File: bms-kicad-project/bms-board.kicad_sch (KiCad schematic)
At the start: 0 parts

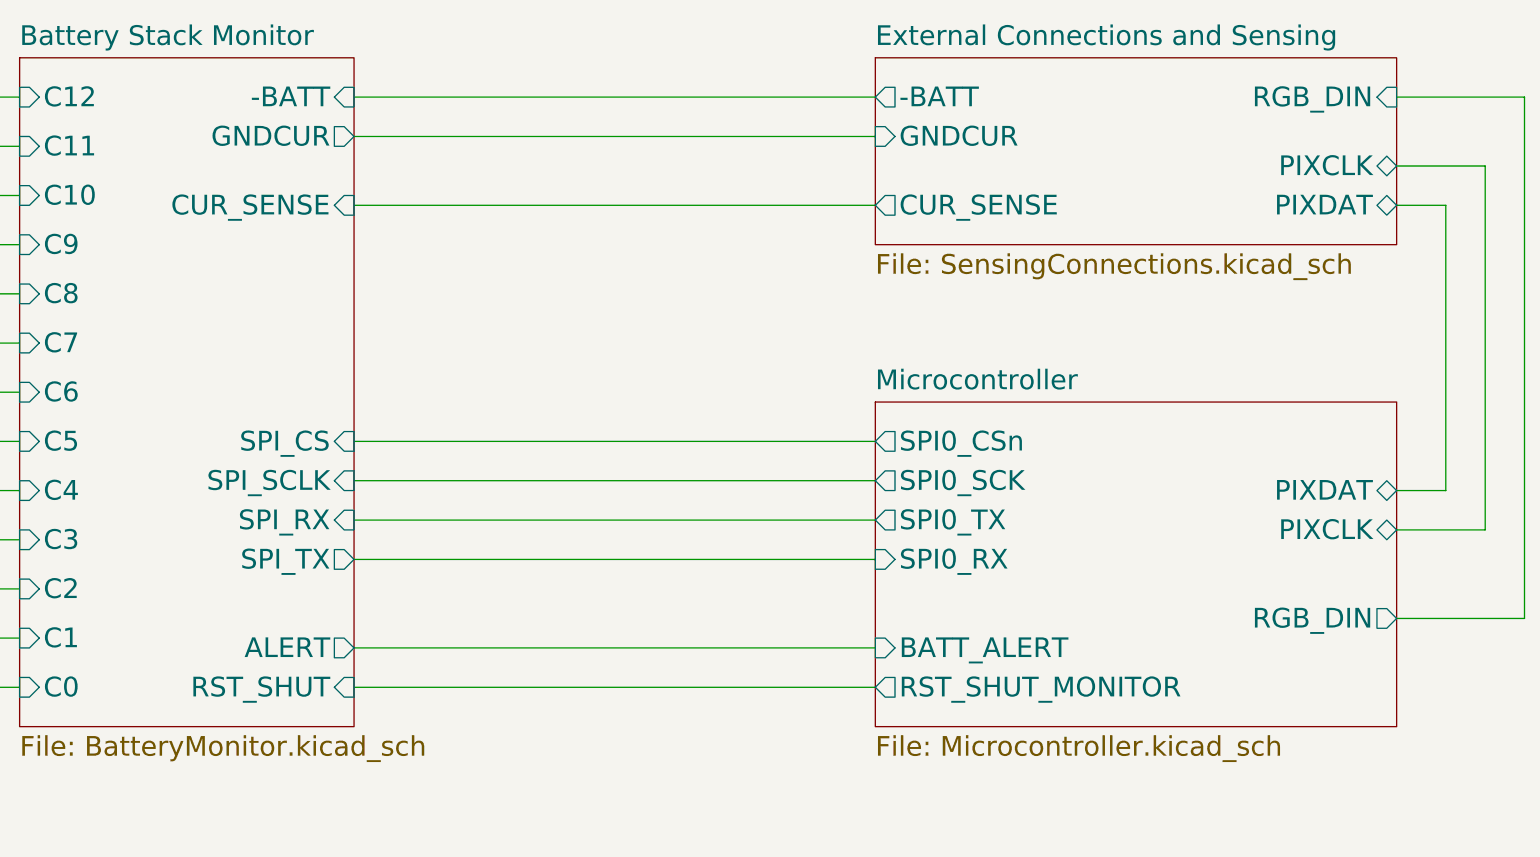
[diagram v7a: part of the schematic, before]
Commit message: feat: added current sense DAC
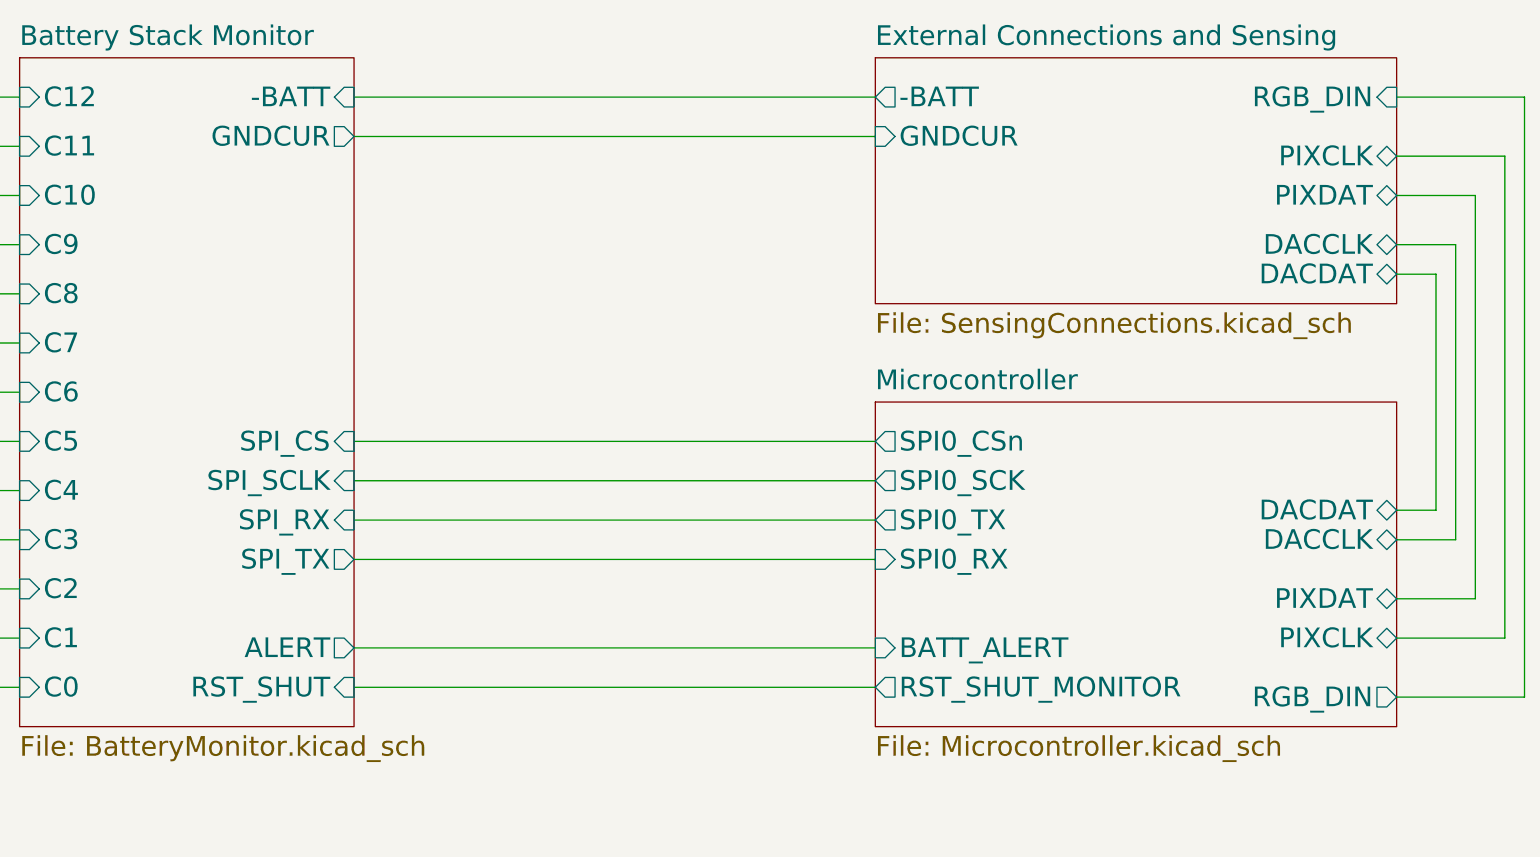
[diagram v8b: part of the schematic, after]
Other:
- sheet Battery Stack Monitor ports: added none; removed CUR_SENSE
- sheet External Connections and Sensing ports: added DACCLK, DACDAT; removed CUR_SENSE
- sheet Microcontroller ports: added DACCLK, DACDAT; removed none
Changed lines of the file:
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@@
+    (stroke (width 0) (type default))
+  )
+  (wire (pts (xy 367.03 99.06) (xy 367.03 137.16))
     (stroke (width 0) (type default))
   )
@@
     (stroke (width 0) (type default))
   )
-  (wire (pts (xy 375.92 80.01) (xy 375.92 147.32))
-    (stroke (width 0) (type default))
-  )
-  (wire (pts (xy 375.92 147.32) (xy 359.41 147.32))
-    (stroke (width 0) (type default))
-  )
-  (wire (pts (xy 370.84 135.89) (xy 370.84 88.9))
+  (wire (pts (xy 359.41 149.86) (xy 373.38 149.86))
+    (stroke (width 0) (type default))
+  )
+  (wire (pts (xy 375.92 80.01) (xy 375.92 157.48))
+    (stroke (width 0) (type default))
+  )
+  (wire (pts (xy 375.92 157.48) (xy 359.41 157.48))
+    (stroke (width 0) (type default))
+  )
+  (wire (pts (xy 373.38 87.63) (xy 373.38 149.86))
     (stroke (width 0) (type default))
   )
@@
     (stroke (width 0) (type default))
   )
-  (wire (pts (xy 365.76 93.98) (xy 365.76 130.81))
+  (wire (pts (xy 369.57 92.71) (xy 369.57 144.78))
     (stroke (width 0) (type default))
   )
@@
     (stroke (width 0) (type default))
   )
+  (wire (pts (xy 364.49 133.35) (xy 359.41 133.35))
+    (stroke (width 0) (type default))
+  )
   (wire (pts (xy 115.57 156.21) (xy 181.61 156.21))
     (stroke (width 0) (type default))
   )
-  (wire (pts (xy 370.84 88.9) (xy 359.41 88.9))
-    (stroke (width 0) (type default))
-  )
-  (wire (pts (xy 359.41 135.89) (xy 370.84 135.89))
-    (stroke (width 0) (type default))
-  )
-  (wire (pts (xy 224.79 93.98) (xy 292.1 93.98))
-    (stroke (width 0) (type default))
-  )
   (wire (pts (xy 224.79 151.13) (xy 292.1 151.13))
     (stroke (width 0) (type default))
   )
+  (wire (pts (xy 359.41 99.06) (xy 367.03 99.06))
+    (stroke (width 0) (type default))
+  )
   (wire (pts (xy 224.79 124.46) (xy 292.1 124.46))
     (stroke (width 0) (type default))
@@
     (stroke (width 0) (type default))
   )
-  (wire (pts (xy 359.41 130.81) (xy 365.76 130.81))
-    (stroke (width 0) (type default))
-  )
-  (wire (pts (xy 359.41 93.98) (xy 365.76 93.98))
+  (wire (pts (xy 359.41 144.78) (xy 369.57 144.78))
+    (stroke (width 0) (type default))
+  )
+  (wire (pts (xy 359.41 87.63) (xy 373.38 87.63))
+    (stroke (width 0) (type default))
+  )
+  (wire (pts (xy 359.41 92.71) (xy 369.57 92.71))
     (stroke (width 0) (type default))
   )
@@
     (stroke (width 0) (type default))
   )
+  (wire (pts (xy 364.49 102.87) (xy 364.49 133.35))
+    (stroke (width 0) (type default))
+  )
   (wire (pts (xy 224.79 156.21) (xy 292.1 156.21))
     (stroke (width 0) (type default))
@@
   )
   (wire (pts (xy 115.57 92.71) (xy 181.61 92.71))
+    (stroke (width 0) (type default))
+  )
+  (wire (pts (xy 359.41 102.87) (xy 364.49 102.87))
+    (stroke (width 0) (type default))
+  )
+  (wire (pts (xy 359.41 137.16) (xy 367.03 137.16))
     (stroke (width 0) (type default))
   )
@@
     )
     (pin "RST_SHUT" input (at 224.79 156.21 0)
-      (effects (font (size 2.54 2.54)) (justify right))
-    )
-    (pin "CUR_SENSE" input (at 224.79 93.98 0)
       (effects (font (size 2.54 2.54)) (justify right))
     )
@@
       (effects (font (size 2.54 2.54)) (justify left))
     )
-    (pin "PIXDAT" bidirectional (at 359.41 130.81 0)
-      (effects (font (size 2.54 2.54)) (justify right))
-    )
-    (pin "PIXCLK" bidirectional (at 359.41 135.89 0)
+    (pin "PIXDAT" bidirectional (at 359.41 144.78 0)
+      (effects (font (size 2.54 2.54)) (justify right))
+    )
+    (pin "PIXCLK" bidirectional (at 359.41 149.86 0)
       (effects (font (size 2.54 2.54)) (justify right))
     )
@@
       (effects (font (size 2.54 2.54)) (justify left))
     )
-    (pin "RGB_DIN" output (at 359.41 147.32 0)
+    (pin "RGB_DIN" output (at 359.41 157.48 0)
+      (effects (font (size 2.54 2.54)) (justify right))
+    )
+    (pin "DACCLK" bidirectional (at 359.41 137.16 0)
+      (effects (font (size 2.54 2.54)) (justify right))
+    )
+    (pin "DACDAT" bidirectional (at 359.41 133.35 0)
       (effects (font (size 2.54 2.54)) (justify right))
     )
@@
     )
   )
-  (sheet (at 292.1 74.93) (size 67.31 24.13) (fields_autoplaced)
+  (sheet (at 292.1 74.93) (size 67.31 31.75) (fields_autoplaced)
     (stroke (width 0.1524) (type solid))
     (fill (color 0 0 0 0.0000))
@@
       (effects (font (size 2.54 2.54)) (justify left bottom))
     )
-    (property "Sheetfile" "SensingConnections.kicad_sch" (at 292.1 100.1526 0)
-      (effects (font (size 2.54 2.54)) (justify left top))
-    )
-    (pin "CUR_SENSE" output (at 292.1 93.98 180)
-      (effects (font (size 2.54 2.54)) (justify left))
-    )
-    (pin "PIXDAT" bidirectional (at 359.41 93.98 0)
-      (effects (font (size 2.54 2.54)) (justify right))
-    )
-    (pin "PIXCLK" bidirectional (at 359.41 88.9 0)
+    (property "Sheetfile" "SensingConnections.kicad_sch" (at 292.1 107.7726 0)
+      (effects (font (size 2.54 2.54)) (justify left top))
+    )
+    (pin "PIXDAT" bidirectional (at 359.41 92.71 0)
+      (effects (font (size 2.54 2.54)) (justify right))
+    )
+    (pin "PIXCLK" bidirectional (at 359.41 87.63 0)
       (effects (font (size 2.54 2.54)) (justify right))
     )
@@
       (effects (font (size 2.54 2.54)) (justify right))
     )
+    (pin "DACDAT" bidirectional (at 359.41 102.87 0)
+      (effects (font (size 2.54 2.54)) (justify right))
+    )
+    (pin "DACCLK" bidirectional (at 359.41 99.06 0)
+      (effects (font (size 2.54 2.54)) (justify right))
+    )
